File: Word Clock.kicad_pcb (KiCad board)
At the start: 2 copper layers, 190.5 x 190.5 mm, 52 parts, among them J1 USB_C_Receptacle_USB2.0, Q1 Q_NMOS_GSD, U1 NUP2202, U2 PIC18LF46K80-IPT, U3 LM1117-3.3, U4 DS3231MZ, U5 FT230XS

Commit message: Added lines in the silk so the LEDs can be placed accurately.
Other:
- board text added: "EIGHT"
- board text added: "ELEVEN"
- board text added: "FIVE"
- board text added: "FOUR"
- board text added: "HALF"
- board text added: "IS"
- board text added: "IT"
- board text added: "MINUTES"
- board text added: "NINE"
- board text added: "OCLOCK"
- board text added: "ONE"
- board text added: "PAST"
- board text added: "QUARTER"
- board text added: "SEVEN"
- board text added: "SIX"
- board text added: "TEN"
- board text added: "THREE"
- board text added: "TO"
- board text added: "TWELVE"
- board text added: "TWENTY"
- board text added: "TWO"
- board text added: "X"

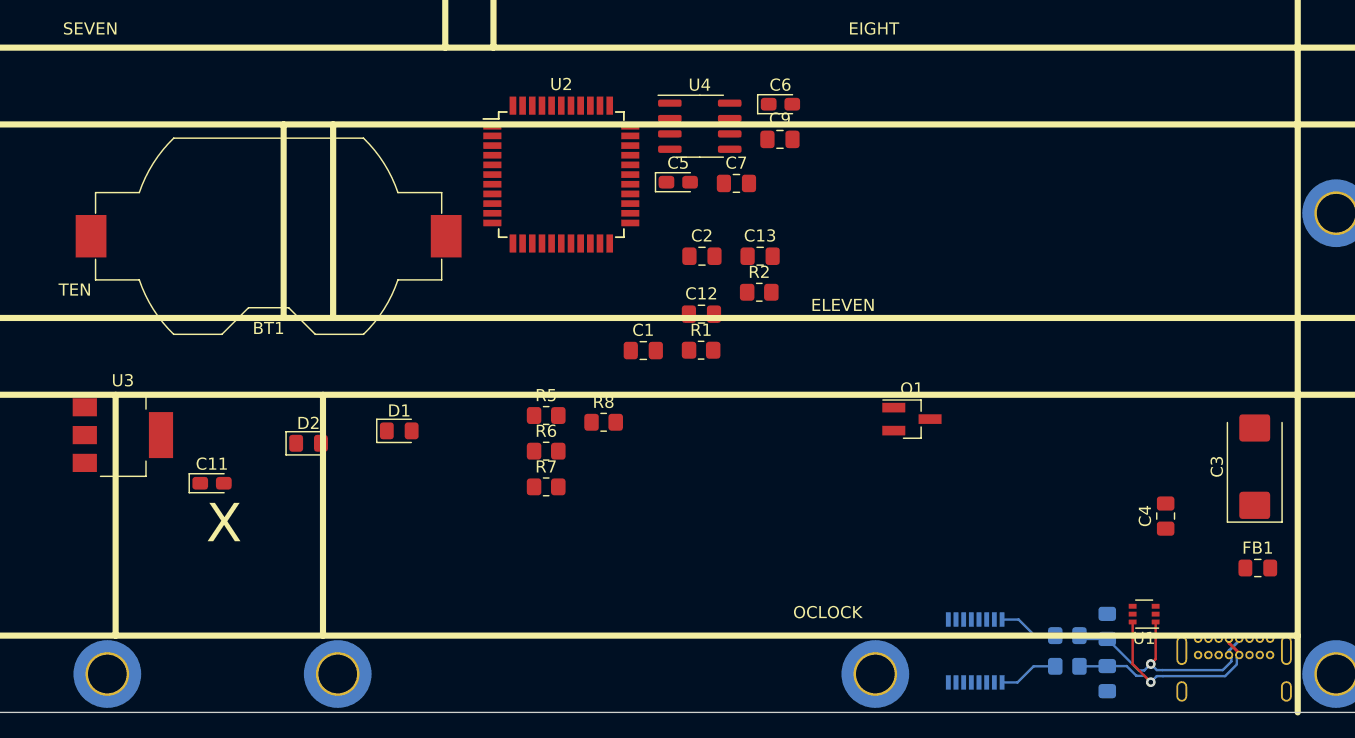
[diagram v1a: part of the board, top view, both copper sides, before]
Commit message: Starting some prelim layout. Perhaps I should finish my schematics and place all my parts first.... But what do I know?
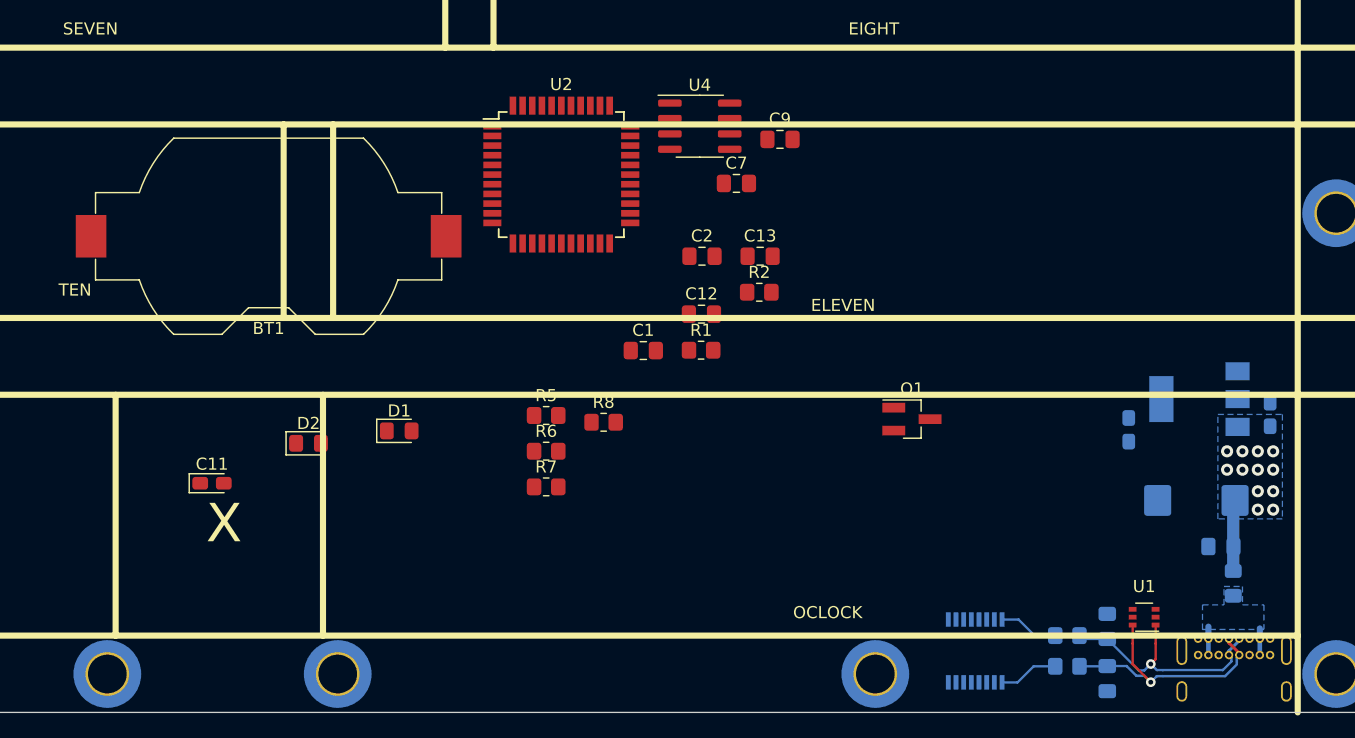
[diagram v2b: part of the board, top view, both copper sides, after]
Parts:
- C3, C4, C5, C6, FB1, U3: moved to B.Cu
- moved U3 89.1 mm to (176.0, -25.9), turned to 180 degrees
- moved C5 52.6 mm to (181.9, -24.6), turned to 90 degrees
- moved C6 39.4 mm to (170.2, -23.4), turned to 270 degrees
- moved C3 5.58 mm to (175.8, -17.5), turned to 180 degrees
- moved C4 5.22 mm to (177.8, -13.7), turned to 180 degrees
- moved FB1 2.40 mm to (178.8, -10.7), turned to 270 degrees
- moved U1 0.25 mm to (171.4, -7.87)
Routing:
- net +5V: track 0.00 -> 5.90 mm, vias 0 -> 12
- net Net-(FB1-Pad2): track 0.00 -> 4.55 mm
- added copper zone on B.Cu, net +5V
- added copper zone on B.Cu, net Net-(FB1-Pad2)
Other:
- copper layers 2 -> 4
